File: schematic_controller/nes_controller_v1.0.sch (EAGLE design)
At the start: 22 parts

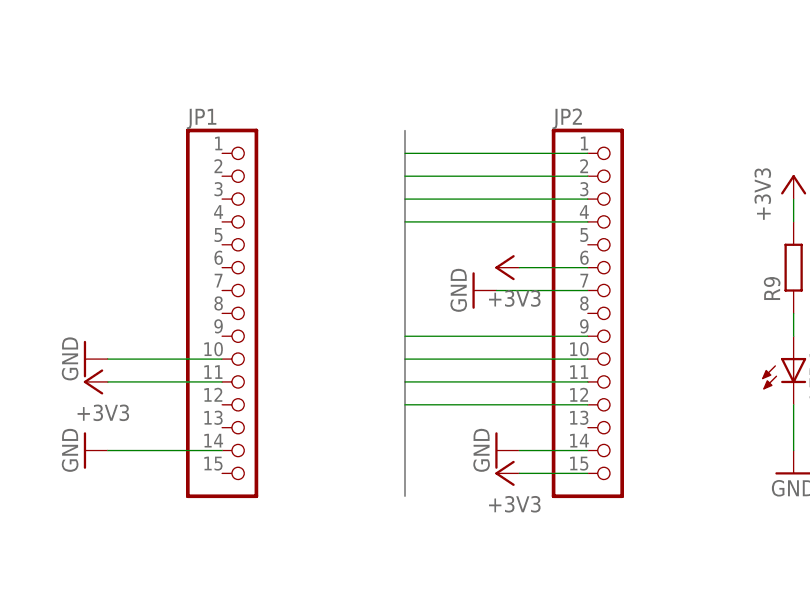
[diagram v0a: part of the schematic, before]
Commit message: updated schematic and board layout to new pin layout
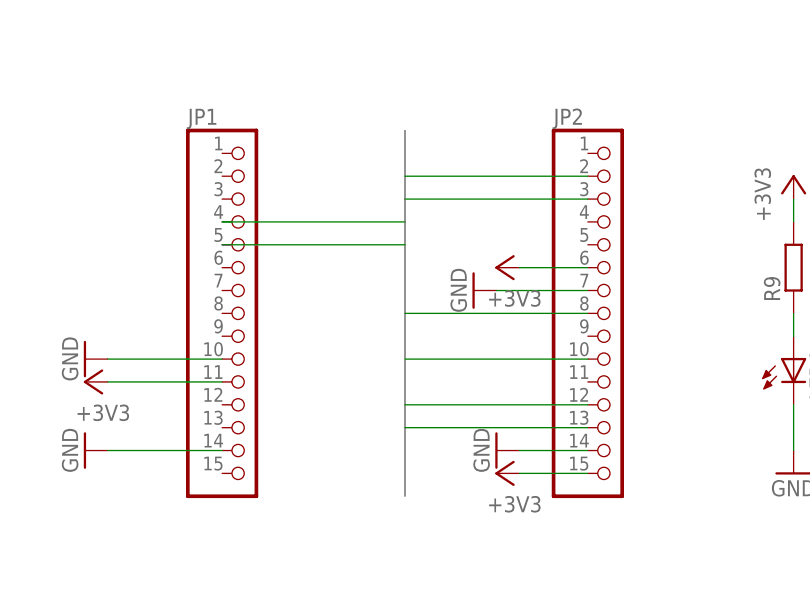
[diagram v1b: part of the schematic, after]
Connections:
- net A: now also JP1.5; no longer JP2.3
- net B: now also JP1.4; no longer JP2.4
- net DOWN: now also JP2.8; no longer JP2.11
- net RIGHT: now also JP2.13; no longer JP2.9
- net SELECT: now also JP2.2; no longer JP2.1
- net START: now also JP2.3; no longer JP2.2
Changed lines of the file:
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@@
 </segment>
 <segment>
-<pinref part="JP2" gate="A" pin="1"/>
-<wire x1="66.04" y1="76.2" x2="86.36" y2="76.2" width="0.1524" layer="91"/>
+<pinref part="JP2" gate="A" pin="2"/>
+<wire x1="86.36" y1="73.66" x2="66.04" y2="73.66" width="0.1524" layer="91"/>
 </segment>
 </net>
@@
 </segment>
 <segment>
-<pinref part="JP2" gate="A" pin="3"/>
-<wire x1="86.36" y1="71.12" x2="66.04" y2="71.12" width="0.1524" layer="91"/>
+<pinref part="JP1" gate="A" pin="5"/>
+<wire x1="45.72" y1="66.04" x2="66.04" y2="66.04" width="0.1524" layer="91"/>
 </segment>
 </net>
@@
 </segment>
 <segment>
-<pinref part="JP2" gate="A" pin="4"/>
-<wire x1="86.36" y1="68.58" x2="66.04" y2="68.58" width="0.1524" layer="91"/>
+<pinref part="JP1" gate="A" pin="4"/>
+<wire x1="45.72" y1="68.58" x2="66.04" y2="68.58" width="0.1524" layer="91"/>
 </segment>
 </net>
@@
 </segment>
 <segment>
-<pinref part="JP2" gate="A" pin="11"/>
-<wire x1="86.36" y1="50.8" x2="66.04" y2="50.8" width="0.1524" layer="91"/>
+<pinref part="JP2" gate="A" pin="8"/>
+<wire x1="86.36" y1="58.42" x2="66.04" y2="58.42" width="0.1524" layer="91"/>
 </segment>
 </net>
@@
 </segment>
 <segment>
-<pinref part="JP2" gate="A" pin="9"/>
-<wire x1="86.36" y1="55.88" x2="66.04" y2="55.88" width="0.1524" layer="91"/>
+<pinref part="JP2" gate="A" pin="13"/>
+<wire x1="86.36" y1="45.72" x2="66.04" y2="45.72" width="0.1524" layer="91"/>
 </segment>
 </net>
@@
 </segment>
 <segment>
-<pinref part="JP2" gate="A" pin="2"/>
-<wire x1="86.36" y1="73.66" x2="66.04" y2="73.66" width="0.1524" layer="91"/>
+<pinref part="JP2" gate="A" pin="3"/>
+<wire x1="86.36" y1="71.12" x2="66.04" y2="71.12" width="0.1524" layer="91"/>
 </segment>
 </net>
